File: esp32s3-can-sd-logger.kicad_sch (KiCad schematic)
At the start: 0 parts

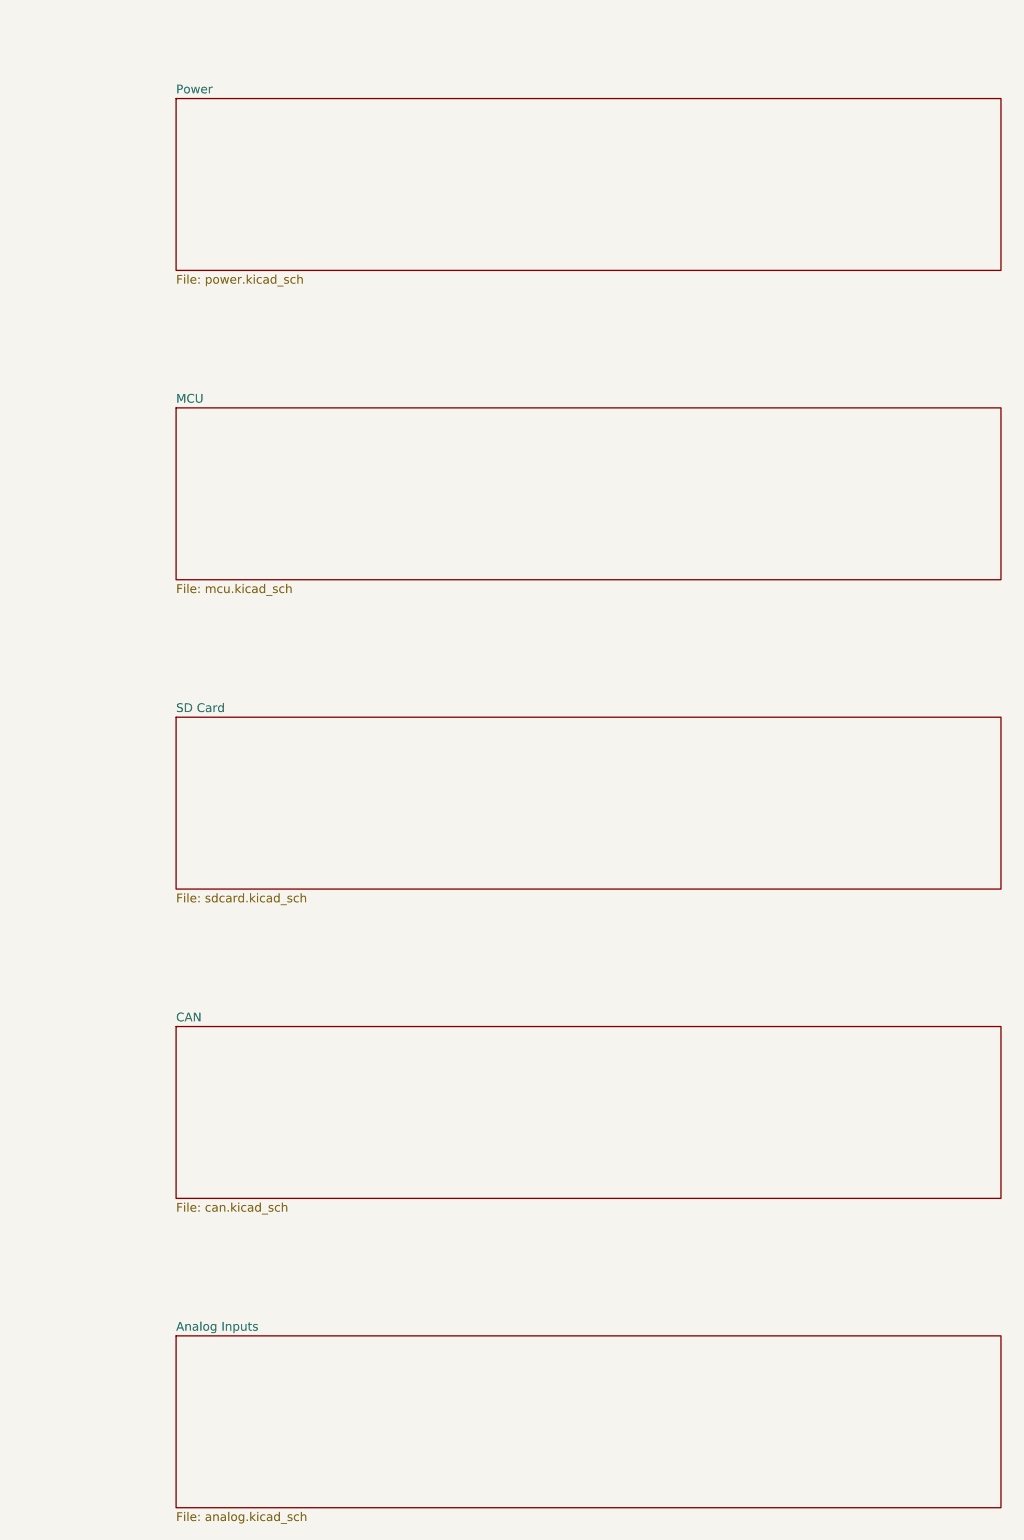
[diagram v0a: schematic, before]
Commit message: Schematic: make the hierarchy real; trunk layout does not decompose
The six sheets were pages, not a hierarchy: every cross-sheet connection
went by global label and no sheet declared an interface. Now the 40 nets
that actually leave a sheet carry hierarchical labels there and appear as
pins on that sheet's symbol at the root, so each block states what it
needs and what it provides. Rails stay global, since a power symbol is
global by definition and does not belong in a signal interface.

Three things had to be right for KiCad to see it, and each announced
itself: dropping both pin labels on a wired net let KiCad autoname it and
validate.py caught the rename; a label anchored 0.6 mm off its wire is a
floating label and ERC said so; and 40 and 32 are not multiples of the
1.27 mm connection grid, so every pin and stub landed off-grid until the
sheets moved to 40.64. The last one hid a real bug -- the sheet symbol
stayed at x=40 while its pins moved to 40.64, leaving them 0.64 mm off
the sheet edge and every one of them unconnected.

On the trunk layout: I measured it rather than attempting it blind, and
it does not decompose into a bounded job. Of ~98 nets, 21 have the
two-pin shape already wired, 40 cross sheets and now have hierarchical
labels, and 37 are multi-pin local nodes -- the ones a person draws as a
wire tree. A trunk needs every part on the node placed against it, but
each two-pin part sits between two different nets, so trunking one net
fixes the position its other net then has to work around. That is
schematic auto-layout, not a special case of it. Restricting to nodes
whose members all end on a rail, which is the one tractable subset, finds
6 of the 37. Six nodes is not worth the machinery, and a half-working
trunk pass would read worse than the honest grid.

Board is untouched by any of this: still 0 DRC errors, 0 unconnected.

Co-Authored-By: Claude Opus 5 <noreply@anthropic.com>
Claude-Session: https://claude.ai/code/session_01DhNbL25h25p8VFCjRfJik9
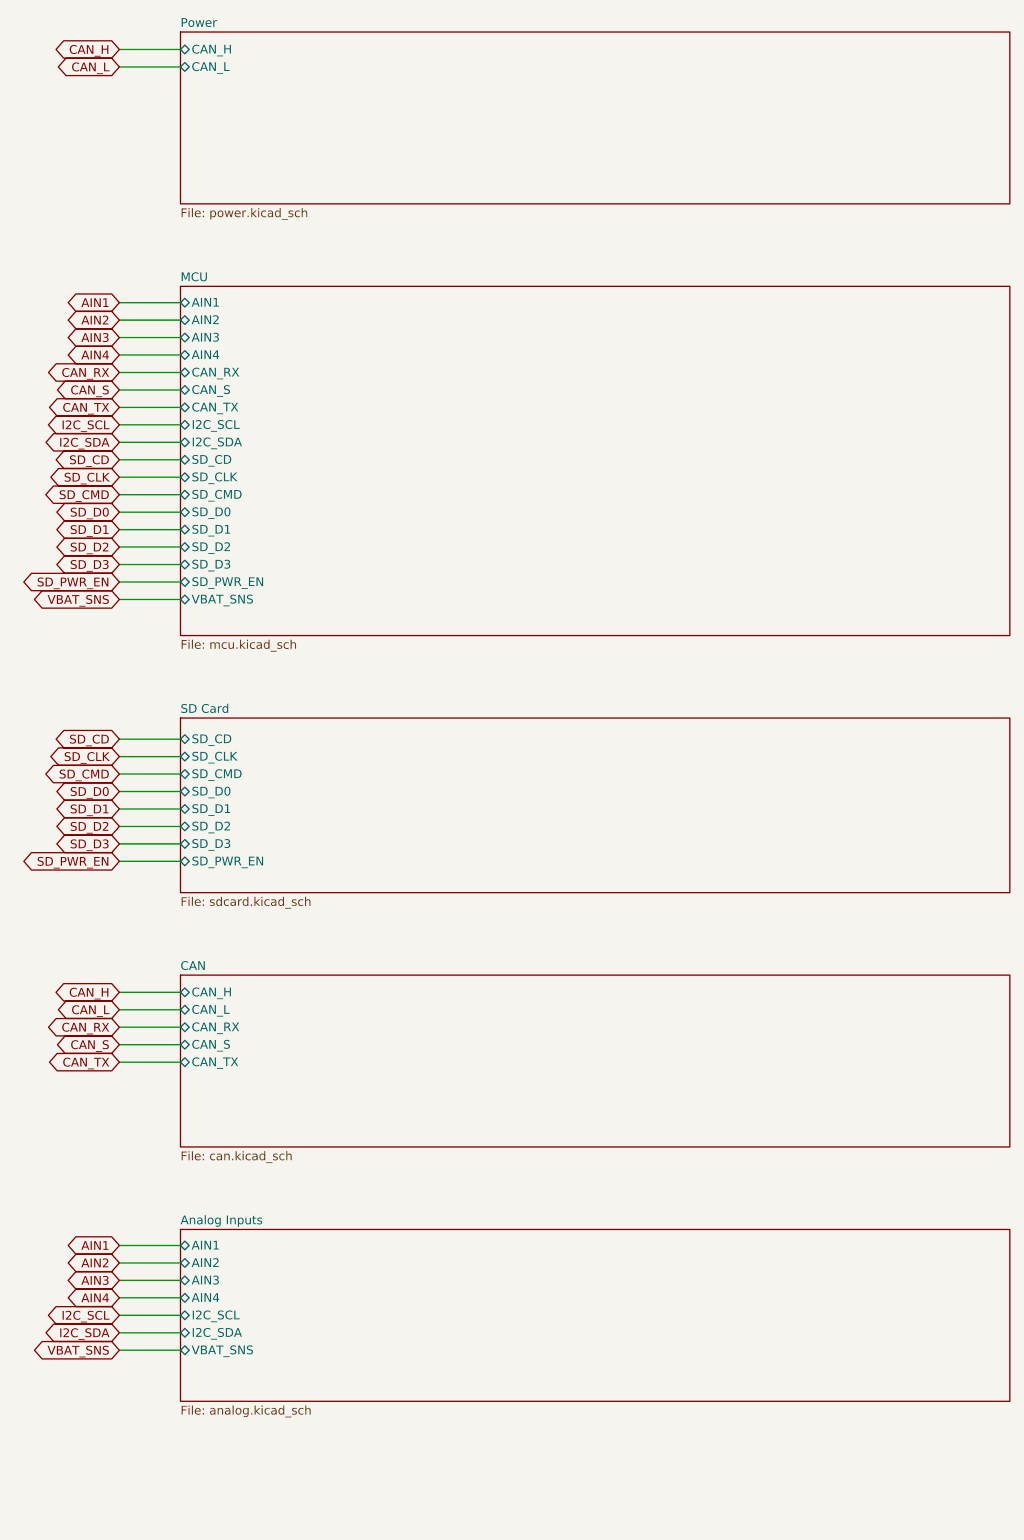
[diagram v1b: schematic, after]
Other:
- sheet Analog Inputs ports: added AIN1, AIN2, AIN3, AIN4, I2C_SCL, I2C_SDA, VBAT_SNS; removed none
- sheet CAN ports: added CAN_H, CAN_L, CAN_RX, CAN_S, CAN_TX; removed none
- sheet MCU ports: added AIN1, AIN2, AIN3, AIN4, CAN_RX, CAN_S, CAN_TX, I2C_SCL, I2C_SDA, SD_CD, SD_CLK, SD_CMD, SD_D0, SD_D1, SD_D2, SD_D3, SD_PWR_EN, VBAT_SNS; removed none
- sheet Power ports: added CAN_H, CAN_L; removed none
- sheet SD Card ports: added SD_CD, SD_CLK, SD_CMD, SD_D0, SD_D1, SD_D2, SD_D3, SD_PWR_EN; removed none

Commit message: Power-fail ride-through: detect, coast, shed; board grows to 84 x 100
The ignition cuts this board's power with a log file open, every drive.
Three new pieces make that survivable, all simulated before layout:

- Detect: TLV431 + 100k/12.7k divider on VBAT_F, AHEAD of the ideal
  diode, asserting PWR_FAIL (IO15) at 11.0 V with ~0.3 V hysteresis.
  The harness collapses microseconds after the key turns while +VBAT
  coasts, so the warning costs no stored energy.
- Coast: two 220 uF/100 V cans join the 100 uF on +VBAT. 540 uF on the
  input rail, where a volt of headroom is worth most.
- Shed: AO3401 + 2N7002 high-side switch on the sensor rail (SENS_EN,
  IO16, off at reset), with PF1 moved behind it so a tripped sensor
  fuse can also be power-cycled from firmware.

Simulated end to end: detection <1 ms after the cut, then 108 ms to
converter dropout with sensors shed, 53 ms without -- the switch doubles
the flush budget. ISO pulse 1's brownout shortens from 8.2 to 5.6 ms.

The two cans plus the detector had no free board left on 84 x 84, so the
board grows to 84 x 100 (still JLC's cheap tier): bottom-edge furniture
and mounting holes move down 16 mm, one can per side, and the detector/
switch column gets its own placement zone. Also included from the audit:
the 3V3 buck's own input capacitor pair at its VIN pin (it was reaching
12.6 mm across to the 5 V island's), the CAN transceiver and AHCT buffer
bypasses pinned at their pins, and Power-class tracks at 0.55 mm to clear
IPC-2221 for 2 A at a 20 C rise.

Hard-won generator fix: a literal newline inside a symbol property is
accepted by KiCad's loader but silently breaks connectivity for every
symbol after it in the file -- the netlist dropped 45 components with no
error pointing anywhere near the cause. The emitter now flattens all
whitespace in property strings.

Board: 0 DRC violations, 0 unconnected, physical audit clean end to end.
185 components, 111 nets, ERC clean, netlist verified node-for-node.

Co-Authore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
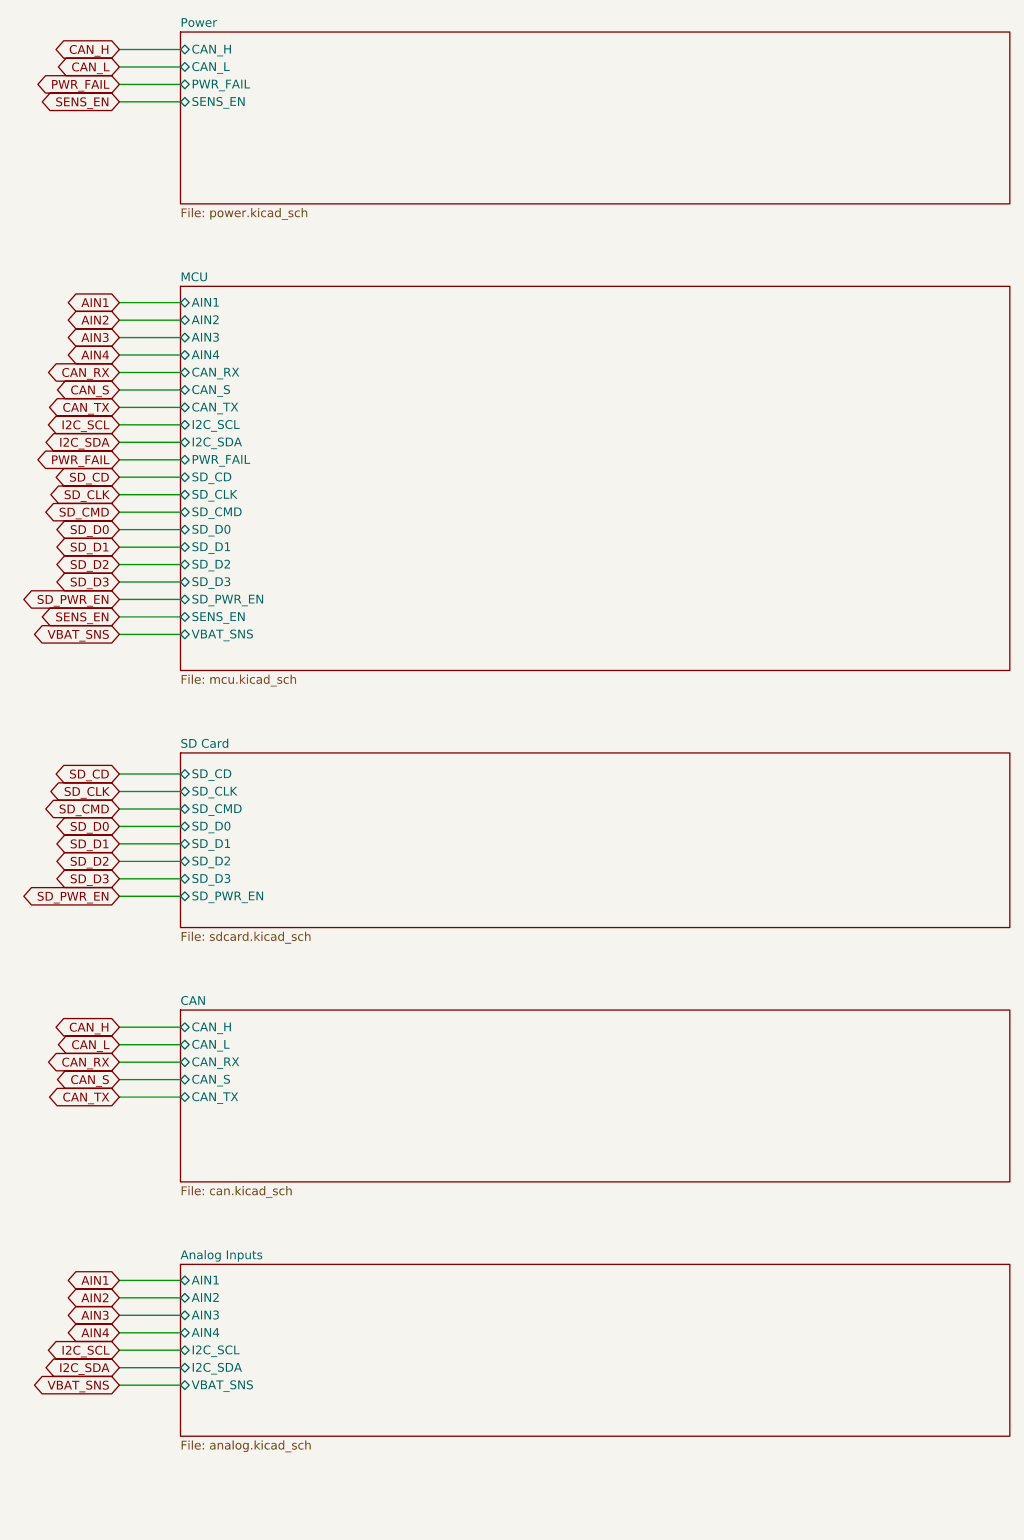
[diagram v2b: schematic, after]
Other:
- sheet MCU ports: added PWR_FAIL, SENS_EN; removed none
- sheet Power ports: added PWR_FAIL, SENS_EN; removed none
